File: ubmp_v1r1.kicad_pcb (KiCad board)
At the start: 2 copper layers, 41.5 x 14 mm, 34 parts, among them J1 Conn_02x05_Counter_Clockwise, J2 USB_A, U1 STM32F103CBUx, U2 MIC5245-3.3, Y1 PRQC8.00CR1010V00L

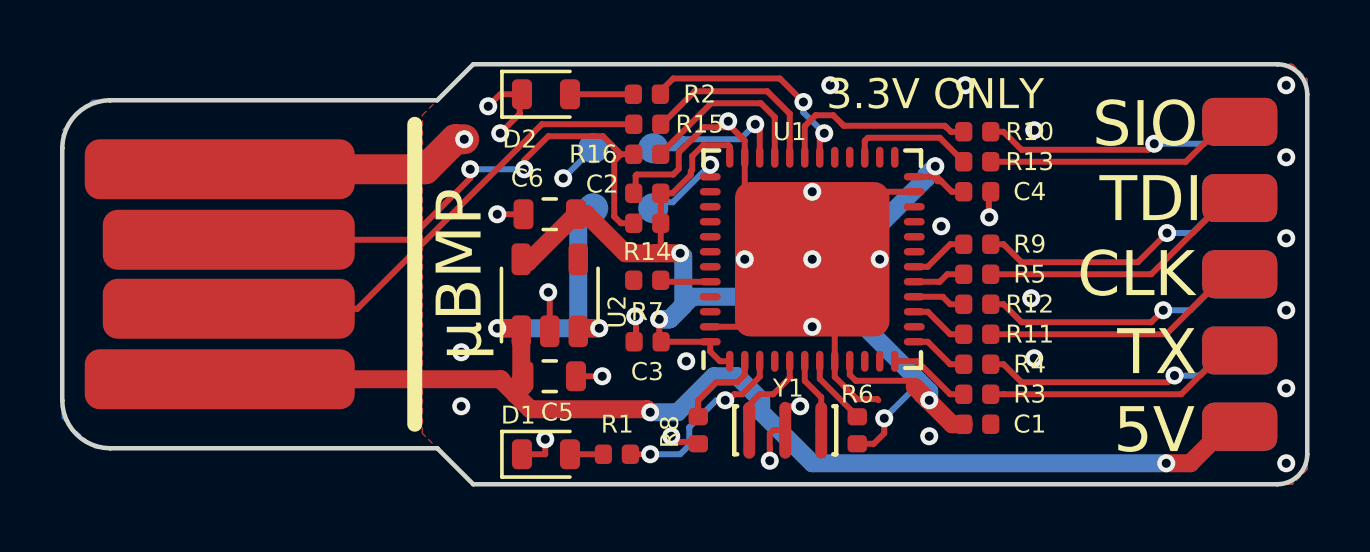
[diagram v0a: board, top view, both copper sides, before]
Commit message: Fixed footprint associations in sch
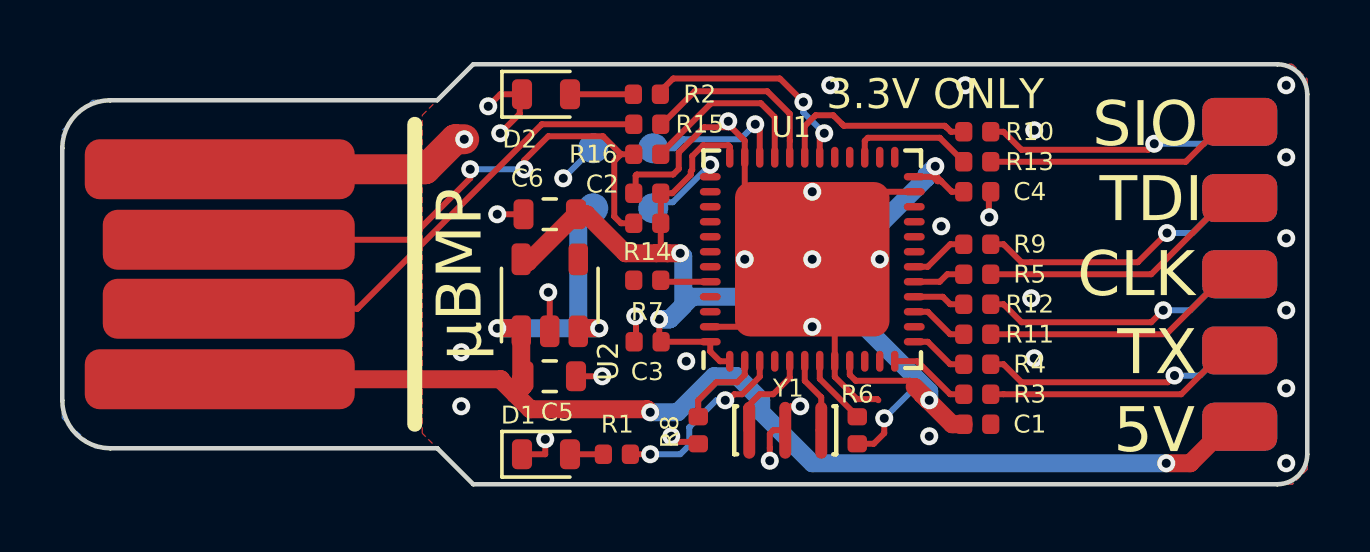
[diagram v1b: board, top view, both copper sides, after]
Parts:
- R1, R2: value 100 -> 470

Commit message: Changed to USB connector, 1.6mm PCB was too thin
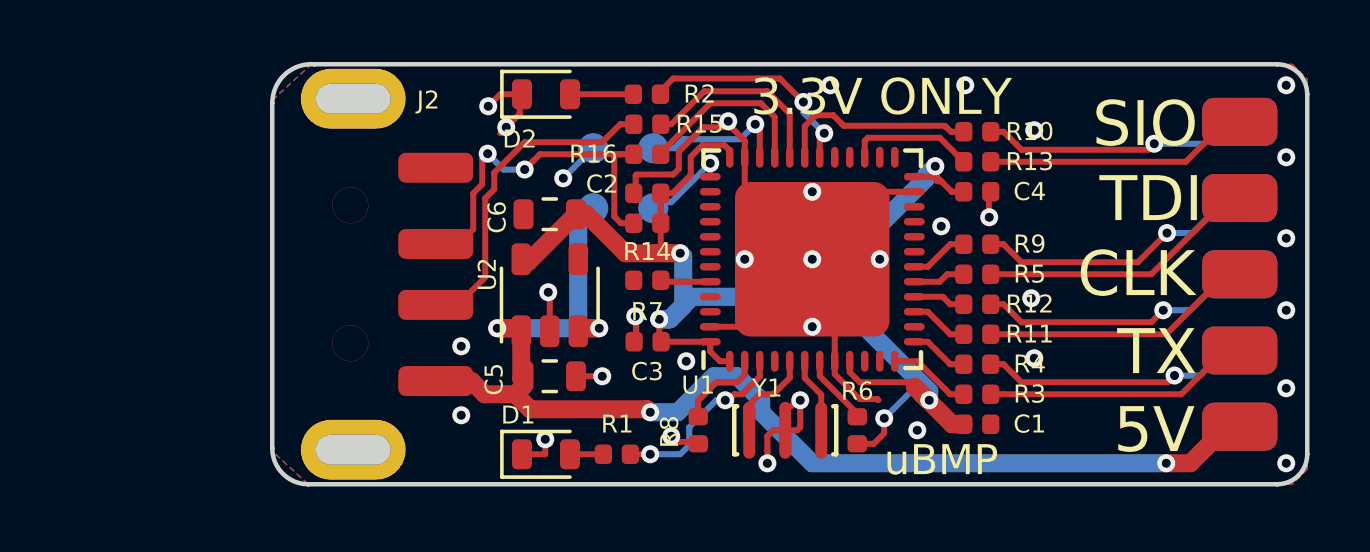
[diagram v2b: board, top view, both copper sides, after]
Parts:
- J2: footprint usbpcb:USBPCB -> usbpcb:USB_A_1001-011-01101
- moved J2 5.20 mm to (89.7, 106.0), turned to 270 degrees
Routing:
- net GND: track 47.2 -> 39.3 mm, vias 35 -> 33
- net +5V: track 47.8 -> 42.0 mm
- net /DP: track 17.6 -> 12.8 mm
- net /DM: track 15.2 -> 11.3 mm
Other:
- board size 41.5 x 14 mm -> 34.5 x 14 mm
- board text added: "uBMP"
- board text removed: "4 Gold fingers"
- board text removed: "µBMP"

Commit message: Changed to USB connector, 1.6mm PCB was too thin
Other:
- outline, holes or cut-outs redrawn
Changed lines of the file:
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@@
     (effects (font (size 1 1) (thickness 0.2)))
   )
-  (gr_line (start 86.95 100.15) (end 88.45 100.15) (layer Edge.Cuts) (width 1))
-  (gr_line (start 86.95 111.85) (end 88.45 111.85) (layer Edge.Cuts) (width 1))
+  (gr_line (start 86.95 100.15) (end 88.45 100.15) (layer F.Fab) (width 1))
+  (gr_line (start 86.95 111.85) (end 88.45 111.85) (layer F.Fab) (width 1))
   (gr_line (start 85 100.3) (end 85 111.8) (layer Edge.Cuts) (width 0.15))
   (gr_arc (start 118.5 112) (end 118.5 113) (angle -90) (layer Edge.Cuts) (width 0.15))
